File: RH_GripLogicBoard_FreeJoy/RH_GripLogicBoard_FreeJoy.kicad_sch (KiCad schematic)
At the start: 21 parts, among them J1 Conn_01x06, J2 Conn_01x06, J3 Conn_01x06, J4 Conn_01x02, J5 Conn_01x02, J6 Conn_01x07, J7 Conn_01x02, J8 Conn_01x02, U1 74HC165, U2 74HC165

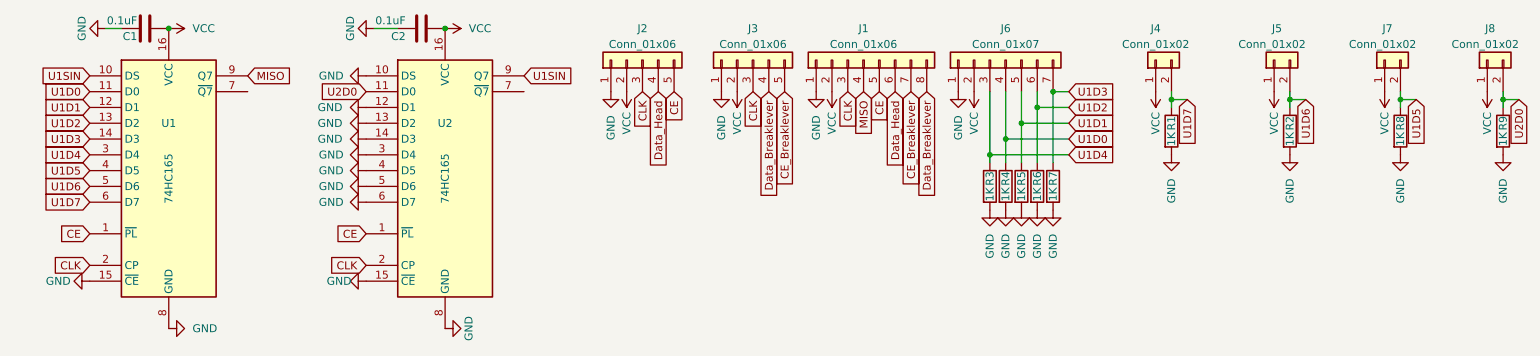
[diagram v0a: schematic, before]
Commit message: fixed mistake in Grip logic pcb's
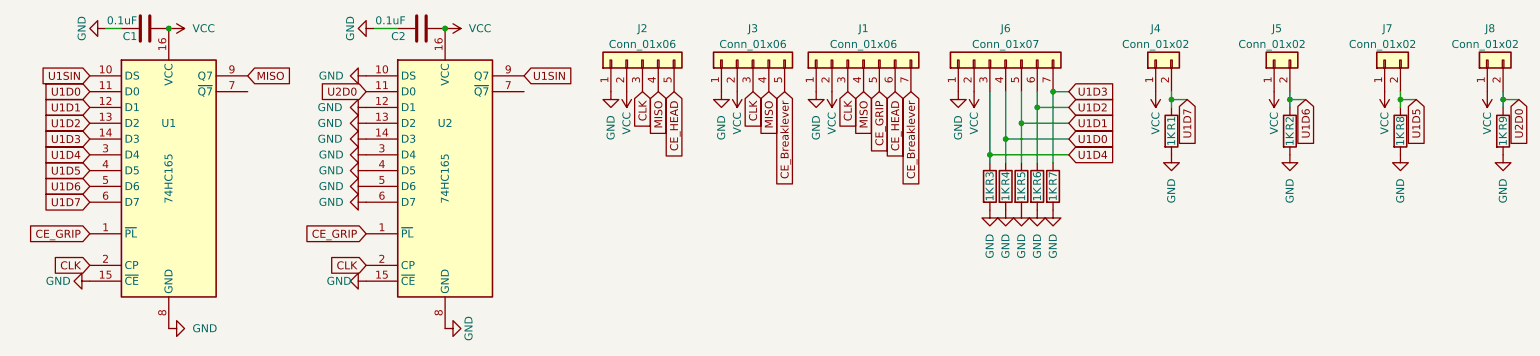
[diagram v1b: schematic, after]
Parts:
- J1: footprint Connector_JST:JST_XH_B8B-XH-A_1x08_P2.50mm_Vertical -> Connector_JST:JST_XH_B7B-XH-A_1x07_P2.50mm_Vertical; symbol Connector_Generic:Conn_01x08 -> Connector_Generic:Conn_01x07
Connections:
- net MISO: now also J2.4 (Pin_4), J3.4 (Pin_4)
- net CE renamed CE_GRIP
- net CE_GRIP: no longer J2.5 (Pin_5)
- removed net Data_Breaklever: J1.8 (Pin_8), J3.4 (Pin_4)
- net Data_Head renamed CE_HEAD
- net CE_HEAD: now also J2.5 (Pin_5); no longer J2.4 (Pin_4)
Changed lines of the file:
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@@
     )
   )
-  (global_label "Data_Head" (shape input) (at 151.13 26.67 270) (fields_autoplaced)
-    (effects (font (size 1.27 1.27)) (justify right))
-    (property "Intersheetrefs" "${INTERSHEET_REFS}" (at 151.13 39.5542 90)
+  (global_label "MISO" (shape input) (at 113.03 26.67 270) (fields_autoplaced)
+    (effects (font (size 1.27 1.27)) (justify right))
+    (property "Intersheetrefs" "${INTERSHEET_REFS}" (at 113.03 34.172 90)
+      (effects (font (size 1.27 1.27)) (justify right) hide)
+    )
+  )
+  (global_label "CE_HEAD" (shape input) (at 151.13 26.67 270) (fields_autoplaced)
+    (effects (font (size 1.27 1.27)) (justify right))
+    (property "Intersheetrefs" "${INTERSHEET_REFS}" (at 151.13 37.8799 90)
       (effects (font (size 1.27 1.27)) (justify right) hide)
     )
@@
     )
   )
-  (global_label "Data_Breaklever" (shape input) (at 156.21 26.67 270) (fields_autoplaced)
-    (effects (font (size 1.27 1.27)) (justify right))
-    (property "Intersheetrefs" "${INTERSHEET_REFS}" (at 156.21 44.7552 90)
-      (effects (font (size 1.27 1.27)) (justify right) hide)
-    )
-  )
   (global_label "U2D0" (shape input) (at 251.46 27.94 270) (fields_autoplaced)
     (effects (font (size 1.27 1.27)) (justify right))
@@
     )
   )
-  (global_label "CE" (shape input) (at 66.04 49.53 180) (fields_autoplaced)
-    (effects (font (size 1.27 1.27)) (justify right))
-    (property "Intersheetrefs" "${INTERSHEET_REFS}" (at 60.7152 49.53 0)
+  (global_label "CE_GRIP" (shape input) (at 66.04 49.53 180) (fields_autoplaced)
+    (effects (font (size 1.27 1.27)) (justify right))
+    (property "Intersheetrefs" "${INTERSHEET_REFS}" (at 55.2534 49.53 0)
       (effects (font (size 1.27 1.27)) (justify right) hide)
     )
@@
     )
   )
-  (global_label "CE" (shape input) (at 148.59 26.67 270) (fields_autoplaced)
-    (effects (font (size 1.27 1.27)) (justify right))
-    (property "Intersheetrefs" "${INTERSHEET_REFS}" (at 148.59 31.9948 90)
+  (global_label "CE_GRIP" (shape input) (at 148.59 26.67 270) (fields_autoplaced)
+    (effects (font (size 1.27 1.27)) (justify right))
+    (property "Intersheetrefs" "${INTERSHEET_REFS}" (at 148.59 37.4566 90)
       (effects (font (size 1.27 1.27)) (justify right) hide)
     )
@@
     )
   )
-  (global_label "CE" (shape input) (at 115.57 26.67 270) (fields_autoplaced)
-    (effects (font (size 1.27 1.27)) (justify right))
-    (property "Intersheetrefs" "${INTERSHEET_REFS}" (at 115.57 31.9948 90)
+  (global_label "CE_HEAD" (shape input) (at 115.57 26.67 270) (fields_autoplaced)
+    (effects (font (size 1.27 1.27)) (justify right))
+    (property "Intersheetrefs" "${INTERSHEET_REFS}" (at 115.57 37.8799 90)
       (effects (font (size 1.27 1.27)) (justify right) hide)
     )
@@
     )
   )
-  (global_label "Data_Breaklever" (shape input) (at 130.81 26.67 270) (fields_autoplaced)
-    (effects (font (size 1.27 1.27)) (justify right))
-    (property "Intersheetrefs" "${INTERSHEET_REFS}" (at 130.81 44.7552 90)
+  (global_label "MISO" (shape input) (at 130.81 26.67 270) (fields_autoplaced)
+    (effects (font (size 1.27 1.27)) (justify right))
+    (property "Intersheetrefs" "${INTERSHEET_REFS}" (at 130.81 34.2514 90)
       (effects (font (size 1.27 1.27)) (justify right) hide)
     )
@@
     )
   )
-  (global_label "Data_Head" (shape input) (at 113.03 26.67 270) (fields_autoplaced)
-    (effects (font (size 1.27 1.27)) (justify right))
-    (property "Intersheetrefs" "${INTERSHEET_REFS}" (at 113.03 39.5542 90)
-      (effects (font (size 1.27 1.27)) (justify right) hide)
-    )
-  )
   (global_label "U1D0" (shape input) (at 21.59 26.67 180) (fields_autoplaced)
     (effects (font (size 1.27 1.27)) (justify right))
@@
     )
   )
-  (global_label "CE" (shape input) (at 21.59 49.53 180) (fields_autoplaced)
-    (effects (font (size 1.27 1.27)) (justify right))
-    (property "Intersheetrefs" "${INTERSHEET_REFS}" (at 16.2652 49.53 0)
+  (global_label "CE_GRIP" (shape input) (at 21.59 49.53 180) (fields_autoplaced)
+    (effects (font (size 1.27 1.27)) (justify right))
+    (property "Intersheetrefs" "${INTERSHEET_REFS}" (at 10.8034 49.53 0)
       (effects (font (size 1.27 1.27)) (justify right) hide)
     )
@@
     )
   )
-  (symbol (lib_id "Connector_Generic:Conn_01x08") (at 146.05 21.59 90) (unit 1)
+  (symbol (lib_id "Connector_Generic:Conn_01x07") (at 146.05 21.59 90) (unit 1)
     (in_bom yes) (on_board yes) (dnp no)
     (property "Reference" "J1" (at 146.05 16.51 90)
@@
       (effects (font (size 1.27 1.27)))
     )
-    (property "Footprint" "Connector_JST:JST_XH_B8B-XH-A_1x08_P2.50mm_Vertical" (at 146.05 21.59 0)
+    (property "Footprint" "Connector_JST:JST_XH_B7B-XH-A_1x07_P2.50mm_Vertical" (at 146.05 21.59 0)
       (effects (font (size 1.27 1.27)) hide)
     )
@@
     (pin "6")
     (pin "7")
-    (pin "8")
-    (instances
-      (project "RH_GripLogicBoard_FreeJoy"
+    (instances
+      (project "RH_GripLogicBoard_FreeJoy"
